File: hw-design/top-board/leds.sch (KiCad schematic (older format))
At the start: 31 parts, among them U4 PCA9685

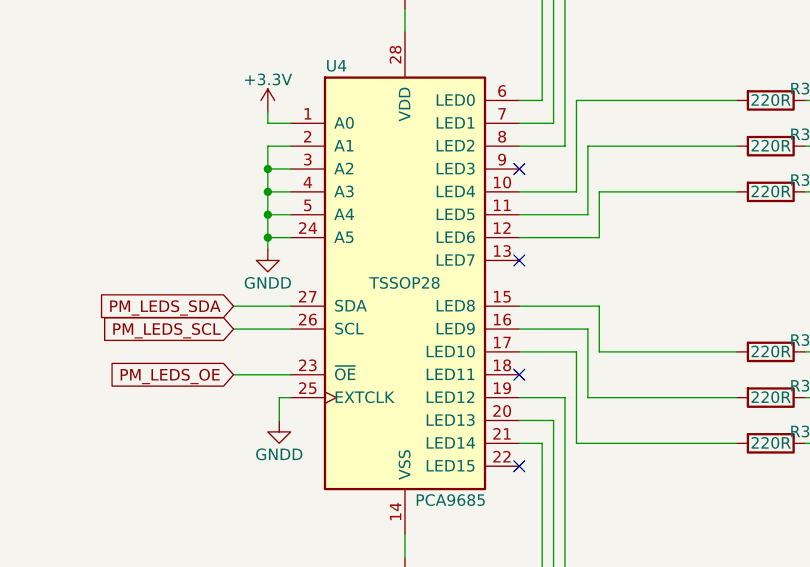
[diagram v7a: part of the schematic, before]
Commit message: sch,top-board: footprints creation/assignment done
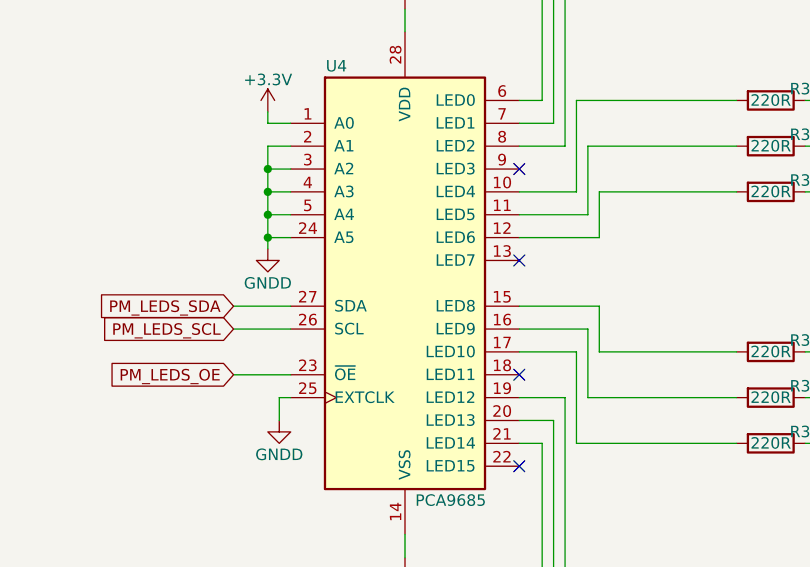
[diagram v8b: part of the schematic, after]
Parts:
- C41, C42, C43, C44, C45, C46: footprint (none) -> Capacitors_SMD:C_0603
- D3, D4, D5, D6, D7, D8: footprint (none) -> LEDs:LED_RGB_PLLC-6
- R24, R25, R26, R27, R28, R29, R30, R31, R32, R33, R34, R35, R36, R37, R38, R39, R40, R41: footprint (none) -> Resistors_SMD:R_0603
- U4: footprint TSSOP28 -> Housings_SSOP:TSSOP-28_4.4x9.7mm_Pitch0.65mm
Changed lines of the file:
@@
 F 0 "D3" H 2800 2500 50  0000 C CNN
 F 1 "LED_RGB" H 2800 2400 50  0000 C CNN
-F 2 "" H 2800 2000 60  0000 C CNN
+F 2 "LEDs:LED_RGB_PLLC-6" H 2800 2000 60  0001 C CNN
 F 3 "" H 2800 2000 60  0000 C CNN
 F 4 "LTRBGFSF-ABCB-QKYO-Z" H 2800 2050 60  0001 C CNN "MPN"
@@
 F 0 "R24" V 2100 2000 50  0000 C CNN
 F 1 "220R" V 2150 1850 50  0000 C CNN
-F 2 "" V 2080 1850 30  0000 C CNN
+F 2 "Resistors_SMD:R_0603" V 2080 1850 30  0001 C CNN
 F 3 "" H 2150 1850 30  0000 C CNN
 F 4 "RMCF0603JT220R" H 0   0   50  0001 C CNN "MPN"
@@
 F 0 "R26" V 2100 2200 50  0000 C CNN
 F 1 "220R" V 2150 2050 50  0000 C CNN
-F 2 "" V 2080 2050 30  0000 C CNN
+F 2 "Resistors_SMD:R_0603" V 2080 2050 30  0001 C CNN
 F 3 "" H 2150 2050 30  0000 C CNN
 F 4 "RMCF0603JT220R" H 0   0   50  0001 C CNN "MPN"
@@
 F 0 "R28" V 2100 2400 50  0000 C CNN
 F 1 "220R" V 2150 2250 50  0000 C CNN
-F 2 "" V 2080 2250 30  0000 C CNN
+F 2 "Resistors_SMD:R_0603" V 2080 2250 30  0001 C CNN
 F 3 "" H 2150 2250 30  0000 C CNN
 F 4 "RMCF0603JT220R" H 0   0   50  0001 C CNN "MPN"
@@
 F 0 "C41" H 3475 2150 50  0000 L CNN
 F 1 "100nF" H 3475 1950 50  0000 L CNN
-F 2 "" H 3488 1900 30  0000 C CNN
+F 2 "Capacitors_SMD:C_0603" H 3488 1900 30  0001 C CNN
 F 3 "" H 3450 2050 60  0000 C CNN
 F 4 "C1608X7R1E104K080AA" H 0   0   50  0001 C CNN "MPN"
@@
 F 0 "D5" H 2800 3600 50  0000 C CNN
 F 1 "LED_RGB" H 2800 3500 50  0000 C CNN
-F 2 "" H 2800 3100 60  0000 C CNN
+F 2 "LEDs:LED_RGB_PLLC-6" H 2800 3100 60  0001 C CNN
 F 3 "" H 2800 3100 60  0000 C CNN
 F 4 "LTRBGFSF-ABCB-QKYO-Z" H 2800 3150 60  0001 C CNN "MPN"
@@
 F 0 "R30" V 2100 3100 50  0000 C CNN
 F 1 "220R" V 2150 2950 50  0000 C CNN
-F 2 "" V 2080 2950 30  0000 C CNN
+F 2 "Resistors_SMD:R_0603" V 2080 2950 30  0001 C CNN
 F 3 "" H 2150 2950 30  0000 C CNN
 F 4 "RMCF0603JT220R" H 0   0   50  0001 C CNN "MPN"
@@
 F 0 "R32" V 2100 3300 50  0000 C CNN
 F 1 "220R" V 2150 3150 50  0000 C CNN
-F 2 "" V 2080 3150 30  0000 C CNN
+F 2 "Resistors_SMD:R_0603" V 2080 3150 30  0001 C CNN
 F 3 "" H 2150 3150 30  0000 C CNN
 F 4 "RMCF0603JT220R" H 0   0   50  0001 C CNN "MPN"
@@
 F 0 "R34" V 2100 3500 50  0000 C CNN
 F 1 "220R" V 2150 3350 50  0000 C CNN
-F 2 "" V 2080 3350 30  0000 C CNN
+F 2 "Resistors_SMD:R_0603" V 2080 3350 30  0001 C CNN
 F 3 "" H 2150 3350 30  0000 C CNN
 F 4 "RMCF0603JT220R" H 0   0   50  0001 C CNN "MPN"
@@
 F 0 "C43" H 3475 3250 50  0000 L CNN
 F 1 "100nF" H 3475 3050 50  0000 L CNN
-F 2 "" H 3488 3000 30  0000 C CNN
+F 2 "Capacitors_SMD:C_0603" H 3488 3000 30  0001 C CNN
 F 3 "" H 3450 3150 60  0000 C CNN
 F 4 "C1608X7R1E104K080AA" H 0   0   50  0001 C CNN "MPN"
@@
 F 0 "C46" H 9675 5450 50  0000 L CNN
 F 1 "100nF" H 9675 5250 50  0000 L CNN
-F 2 "" H 9688 5200 30  0000 C CNN
+F 2 "Capacitors_SMD:C_0603" H 9688 5200 30  0001 C CNN
 F 3 "" H 9650 5350 60  0000 C CNN
 F 4 "C1608X7R1E104K080AA" H 0   0   50  0001 C CNN "MPN"
@@
 F 0 "R41" V 8300 5700 50  0000 C CNN
 F 1 "220R" V 8350 5550 50  0000 C CNN
-F 2 "" V 8280 5550 30  0000 C CNN
+F 2 "Resistors_SMD:R_0603" V 8280 5550 30  0001 C CNN
 F 3 "" H 8350 5550 30  0000 C CNN
 F 4 "RMCF0603JT220R" H 0   0   50  0001 C CNN "MPN"
@@
 F 0 "R40" V 8300 5500 50  0000 C CNN
 F 1 "220R" V 8350 5350 50  0000 C CNN
-F 2 "" V 8280 5350 30  0000 C CNN
+F 2 "Resistors_SMD:R_0603" V 8280 5350 30  0001 C CNN
 F 3 "" H 8350 5350 30  0000 C CNN
 F 4 "RMCF0603JT220R" H 0   0   50  0001 C CNN "MPN"
@@
 F 0 "R39" V 8300 5300 50  0000 C CNN
 F 1 "220R" V 8350 5150 50  0000 C CNN
-F 2 "" V 8280 5150 30  0000 C CNN
+F 2 "Resistors_SMD:R_0603" V 8280 5150 30  0001 C CNN
 F 3 "" H 8350 5150 30  0000 C CNN
 F 4 "RMCF0603JT220R" H 0   0   50  0001 C CNN "MPN"
@@
 F 0 "D8" H 9000 5800 50  0000 C CNN
 F 1 "LED_RGB" H 9000 5700 50  0000 C CNN
-F 2 "" H 9000 5300 60  0000 C CNN
+F 2 "LEDs:LED_RGB_PLLC-6" H 9000 5300 60  0001 C CNN
 F 3 "" H 9000 5300 60  0000 C CNN
 F 4 "LTRBGFSF-ABCB-QKYO-Z" H 9000 5350 60  0001 C CNN "MPN"
@@
 F 0 "C45" H 9675 4350 50  0000 L CNN
 F 1 "100nF" H 9675 4150 50  0000 L CNN
-F 2 "" H 9688 4100 30  0000 C CNN
+F 2 "Capacitors_SMD:C_0603" H 9688 4100 30  0001 C CNN
 F 3 "" H 9650 4250 60  0000 C CNN
 F 4 "C1608X7R1E104K080AA" H 0   0   50  0001 C CNN "MPN"
@@
 F 0 "R38" V 8300 4600 50  0000 C CNN
 F 1 "220R" V 8350 4450 50  0000 C CNN
-F 2 "" V 8280 4450 30  0000 C CNN
+F 2 "Resistors_SMD:R_0603" V 8280 4450 30  0001 C CNN
 F 3 "" H 8350 4450 30  0000 C CNN
 F 4 "RMCF0603JT220R" H 0   0   50  0001 C CNN "MPN"
@@
 F 0 "R37" V 8300 4400 50  0000 C CNN
 F 1 "220R" V 8350 4250 50  0000 C CNN
-F 2 "" V 8280 4250 30  0000 C CNN
+F 2 "Resistors_SMD:R_0603" V 8280 4250 30  0001 C CNN
 F 3 "" H 8350 4250 30  0000 C CNN
 F 4 "RMCF0603JT220R" H 0   0   50  0001 C CNN "MPN"
@@
 F 0 "R36" V 8300 4200 50  0000 C CNN
 F 1 "220R" V 8350 4050 50  0000 C CNN
-F 2 "" V 8280 4050 30  0000 C CNN
+F 2 "Resistors_SMD:R_0603" V 8280 4050 30  0001 C CNN
 F 3 "" H 8350 4050 30  0000 C CNN
 F 4 "RMCF0603JT220R" H 0   0   50  0001 C CNN "MPN"
@@
 F 0 "D7" H 9000 4700 50  0000 C CNN
 F 1 "LED_RGB" H 9000 4600 50  0000 C CNN
-F 2 "" H 9000 4200 60  0000 C CNN
+F 2 "LEDs:LED_RGB_PLLC-6" H 9000 4200 60  0001 C CNN
 F 3 "" H 9000 4200 60  0000 C CNN
 F 4 "LTRBGFSF-ABCB-QKYO-Z" H 9000 4250 60  0001 C CNN "MPN"
@@
 F 0 "C44" H 9675 3250 50  0000 L CNN
 F 1 "100nF" H 9675 3050 50  0000 L CNN
-F 2 "" H 9688 3000 30  0000 C CNN
+F 2 "Capacitors_SMD:C_0603" H 9688 3000 30  0001 C CNN
 F 3 "" H 9650 3150 60  0000 C CNN
 F 4 "C1608X7R1E104K080AA" H 0   0   50  0001 C CNN "MPN"
@@
 F 0 "R35" V 8300 3500 50  0000 C CNN
 F 1 "220R" V 8350 3350 50  0000 C CNN
-F 2 "" V 8280 3350 30  0000 C CNN
+F 2 "Resistors_SMD:R_0603" V 8280 3350 30  0001 C CNN
 F 3 "" H 8350 3350 30  0000 C CNN
 F 4 "RMCF0603JT220R" H 0   0   50  0001 C CNN "MPN"
@@
 F 0 "R33" V 8300 3300 50  0000 C CNN
 F 1 "220R" V 8350 3150 50  0000 C CNN
-F 2 "" V 8280 3150 30  0000 C CNN
+F 2 "Resistors_SMD:R_0603" V 8280 3150 30  0001 C CNN
 F 3 "" H 8350 3150 30  0000 C CNN
 F 4 "RMCF0603JT220R" H 0   0   50  0001 C CNN "MPN"
@@
 F 0 "R31" V 8300 3100 50  0000 C CNN
 F 1 "220R" V 8350 2950 50  0000 C CNN
-F 2 "" V 8280 2950 30  0000 C CNN
+F 2 "Resistors_SMD:R_0603" V 8280 2950 30  0001 C CNN
 F 3 "" H 8350 2950 30  0000 C CNN
 F 4 "RMCF0603JT220R" H 0   0   50  0001 C CNN "MPN"
@@
 F 0 "D6" H 9000 3600 50  0000 C CNN
 F 1 "LED_RGB" H 9000 3500 50  0000 C CNN
-F 2 "" H 9000 3100 60  0000 C CNN
+F 2 "LEDs:LED_RGB_PLLC-6" H 9000 3100 60  0001 C CNN
 F 3 "" H 9000 3100 60  0000 C CNN
 F 4 "LTRBGFSF-ABCB-QKYO-Z" H 9000 3150 60  0001 C CNN "MPN"
@@
 F 0 "C42" H 9675 2150 50  0000 L CNN
 F 1 "100nF" H 9675 1950 50  0000 L CNN
-F 2 "" H 9688 1900 30  0000 C CNN
+F 2 "Capacitors_SMD:C_0603" H 9688 1900 30  0001 C CNN
 F 3 "" H 9650 2050 60  0000 C CNN
 F 4 "C1608X7R1E104K080AA" H 0   0   50  0001 C CNN "MPN"
@@
 F 0 "R29" V 8300 2400 50  0000 C CNN
 F 1 "220R" V 8350 2250 50  0000 C CNN
-F 2 "" V 8280 2250 30  0000 C CNN
+F 2 "Resistors_SMD:R_0603" V 8280 2250 30  0001 C CNN
 F 3 "" H 8350 2250 30  0000 C CNN
 F 4 "RMCF0603JT220R" H 0   0   50  0001 C CNN "MPN"
@@
 F 0 "R27" V 8300 2200 50  0000 C CNN
 F 1 "220R" V 8350 2050 50  0000 C CNN
-F 2 "" V 8280 2050 30  0000 C CNN
+F 2 "Resistors_SMD:R_0603" V 8280 2050 30  0001 C CNN
 F 3 "" H 8350 2050 30  0000 C CNN
 F 4 "RMCF0603JT220R" H 0   0   50  0001 C CNN "MPN"
@@
 F 0 "R25" V 8300 2000 50  0000 C CNN
 F 1 "220R" V 8350 1850 50  0000 C CNN
-F 2 "" V 8280 1850 30  0000 C CNN
+F 2 "Resistors_SMD:R_0603" V 8280 1850 30  0001 C CNN
 F 3 "" H 8350 1850 30  0000 C CNN
 F 4 "RMCF0603JT220R" H 0   0   50  0001 C CNN "MPN"
@@
 F 0 "D4" H 9000 2500 50  0000 C CNN
 F 1 "LED_RGB" H 9000 2400 50  0000 C CNN
-F 2 "" H 9000 2000 60  0000 C CNN
+F 2 "LEDs:LED_RGB_PLLC-6" H 9000 2000 60  0001 C CNN
 F 3 "" H 9000 2000 60  0000 C CNN
 F 4 "LTRBGFSF-ABCB-QKYO-Z" H 9000 2050 60  0001 C CNN "MPN"
@@
 F 0 "U4" H 6450 4700 50  0000 C CNN
 F 1 "PCA9685" H 6950 2800 50  0000 C CNN
-F 2 "TSSOP28" H 6750 3750 50  0000 C CNN
+F 2 "Housings_SSOP:TSSOP-28_4.4x9.7mm_Pitch0.65mm" H 6750 3750 50  0001 C CNN
 F 3 "" H 6750 3750 60  0000 C CNN
 F 4 "PCA9685PW,112" H 0   0   50  0001 C CNN "MPN"
